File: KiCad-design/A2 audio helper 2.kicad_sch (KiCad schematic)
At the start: 33 parts, among them J1 PIN HEADER 1x2, J10 PIN HEADER 1x3, J11 PIN HEADER 1x3, J12 PIN HEADER 1x3, J19 PIN HEADER 1x4, J2 PIN HEADER 1x2, J3 PIN HEADER 1x2, J4 SJ1-3515N, J5 PIN HEADER 1x3, J6 PIN HEADER 1x3, J7 SJ1-3515N, J9 PIN HEADER 1x5, K1 SR11-5V-200-2C, SW2 SW_DPDT_x2, U1 pam8403

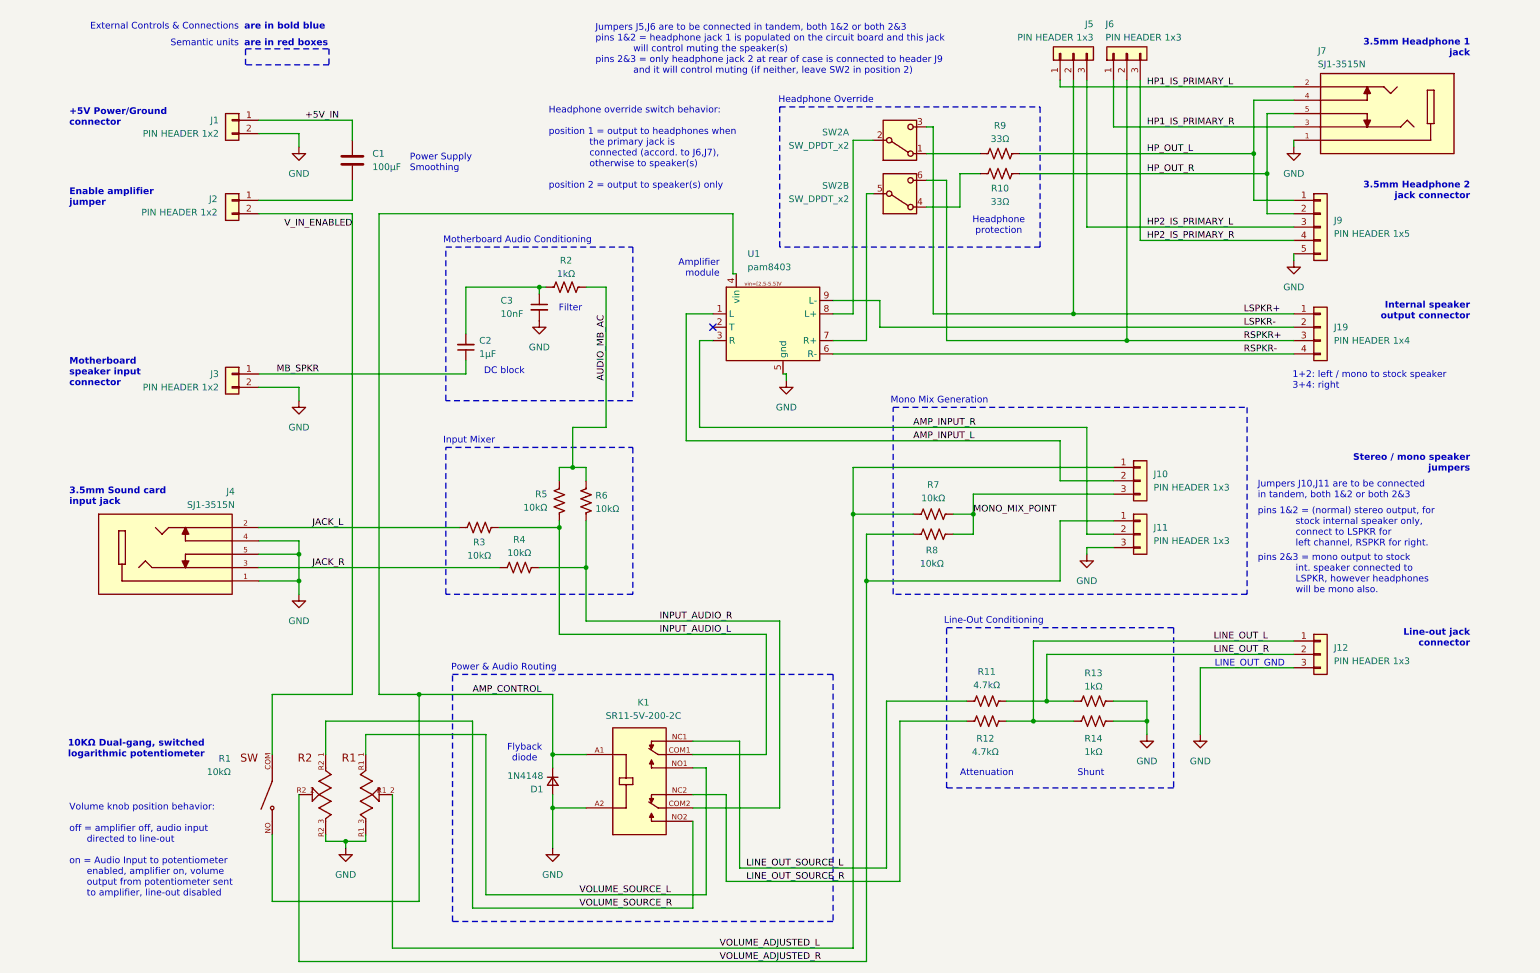
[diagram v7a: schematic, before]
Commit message: picked new connectors, pcb take 2
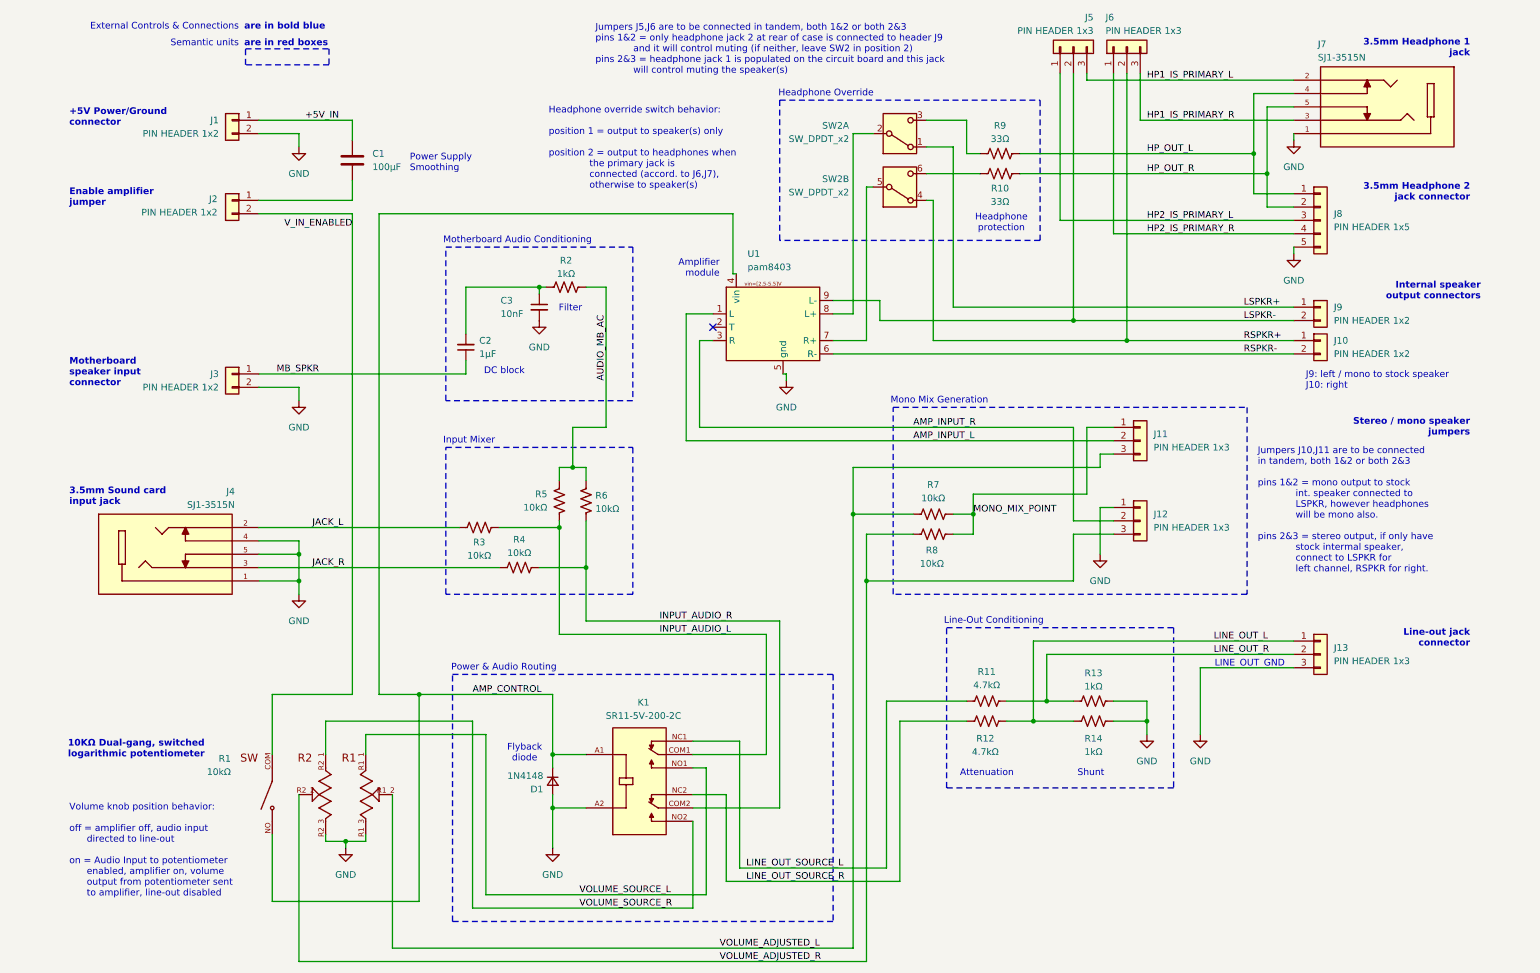
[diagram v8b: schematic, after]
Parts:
- removed J19: PIN HEADER 1x4, Connector_PinHeader_2.54mm:PinHeader_1x04_P2.54mm_Horizontal, symbol Connector_Generic:Conn_01x04
- added J10, J9: PIN HEADER 1x2, Connector_Molex:Molex_KK-254_AE-6410-02A_1x02_P2.54mm_Vertical, symbol Connector_Generic:Conn_01x02
- J1: footprint Connector_Molex:Molex_KK-254_AE-6410-02A_1x02_P2.54mm_Vertical -> footprints:CONN_22035025_MOL
- J13: renamed from J12; footprint Connector_PinHeader_2.54mm:PinHeader_1x03_P2.54mm_Horizontal -> Connector_Molex:Molex_KK-254_AE-6410-03A_1x03_P2.54mm_Vertical
- J3: footprint Connector_PinHeader_2.54mm:PinHeader_1x02_P2.54mm_Horizontal -> Connector_Molex:Molex_KK-254_AE-6410-02A_1x02_P2.54mm_Vertical
- J8: renamed from J9; footprint Connector_PinHeader_2.54mm:PinHeader_1x05_P2.54mm_Horizontal -> Connector_Molex:Molex_KK-254_AE-6410-05A_1x05_P2.54mm_Vertical
- renumbered J10 to J11, J11 to J12
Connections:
- net GND: now also J12.1 (Pin_1); no longer J12.3 (Pin_3)
- net HP1_IS_PRIMARY_L: now also J5.3 (Pin_3); no longer J5.1 (Pin_1)
- net HP1_IS_PRIMARY_R: now also J6.3 (Pin_3); no longer J6.1 (Pin_1)
- net HP2_IS_PRIMARY_L: now also J5.1 (Pin_1); no longer J5.3 (Pin_3)
- net HP2_IS_PRIMARY_R: now also J6.1 (Pin_1); no longer J6.3 (Pin_3)
- net LSPKR+: now also SW2.1 (A), J9.1 (Pin_1); no longer J5.2 (Pin_2), SW2.3 (C)
- net LSPKR-: now also J5.2 (Pin_2), J9.2 (Pin_2)
- net MONO_MIX_POINT: now also J11.1 (Pin_1); no longer J11.3 (Pin_3)
- net RSPKR+: now also SW2.4 (A), J10.1 (Pin_1); no longer SW2.6 (C)
- net RSPKR-: now also J10.2 (Pin_2)
- net VOLUME_ADJUSTED_L: now also J11.3 (Pin_3); no longer J11.1 (Pin_1)
- net VOLUME_ADJUSTED_R: now also J12.3 (Pin_3); no longer J12.1 (Pin_1)
- net at R10.1: now also SW2.6 (C); no longer SW2.4 (A)
- net at R9.1: now also SW2.3 (C); no longer SW2.1 (A)
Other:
- note added: "Headphone override switch behavior: position 1 = output to speaker(s) only position 2 = output to headphones when the primary jack is connected (accord. to J6,J7), otherwise to speaker(s)"
- note added: "Internal speaker output connectors"
- note added: "J9: left / mono to stock speaker J10: right"
- note added: "Jumpers J10,J11 are to be connected in tandem, both 1&2 or both 2&3 pins 1&2 = mono output to stock int. speaker connected to LSPKR, however headphones will be mono also. pins 2&3 = stereo output, if only have stock intermal speaker, connect to LSPKR for left channel, RSPKR for right."
- note added: "Jumpers J5,J6 are to be connected in tandem, both 1&2 or both 2&3 pins 1&2 = only headphone jack 2 at rear of case is connected to header J9 and it will control muting (if neither, leave SW2 in position 2) pins 2&3 = headphone jack 1 is populated on the circuit board and this jack will control muting the speaker(s)"
- note removed: "1+2: left / mono to stock speaker 3+4: right"
- note removed: "Headphone override switch behavior: position 1 = output to headphones when the primary jack is connected (accord. to J6,J7), otherwise to speaker(s) position 2 = output to speaker(s) only"
- note removed: "Internal speaker output connector"
- note removed: "Jumpers J10,J11 are to be connected in tandem, both 1&2 or both 2&3"
- note removed: "Jumpers J5,J6 are to be connected in tandem, both 1&2 or both 2&3 pins 1&2 = headphone jack 1 is populated on the circuit board and this jack will control muting the speaker(s) pins 2&3 = only headphone jack 2 at rear of case is connected to header J9 and it will control muting (if neither, leave SW2 in position 2)"
- note removed: "pins 1&2 = (normal) stereo output, for stock internal speaker only, connect to LSPKR for left channel, RSPKR for right."
- note removed: "pins 2&3 = mono output to stock int. speaker connected to LSPKR, however headphones will be mono also."
- moved on the sheet: J11, J12, J5, J6, J7, J8, SW2A, SW2B
